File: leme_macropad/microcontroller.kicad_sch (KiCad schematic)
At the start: 23 parts, among them U3 W25Q128JVS, U4 RP2040, Y1 ABM8-272-T3

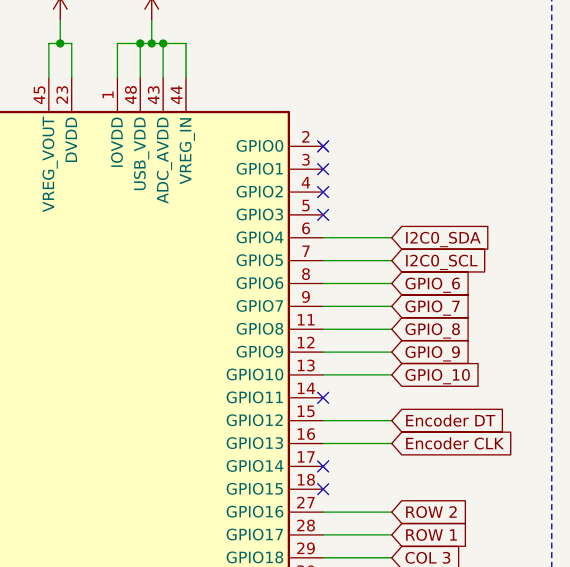
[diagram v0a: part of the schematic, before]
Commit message: Removes unused tespoints
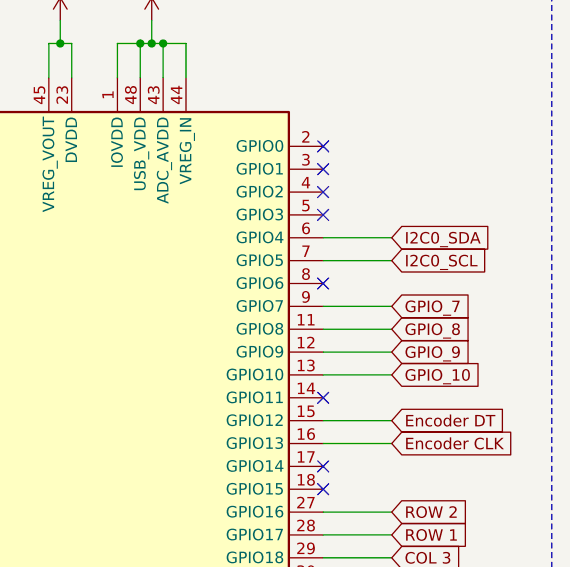
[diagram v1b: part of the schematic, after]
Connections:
- net GPIO_6: no longer names the net of U4.8 (GPIO6)
- no-connect marks 14 -> 15
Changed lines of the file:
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@@
+	)
+	(no_connect
+		(at 256.54 68.58)
 	)
 	(no_connect
@@
 	(wire
 		(pts
-			(xy 256.54 68.58) (xy 264.16 68.58)
-		)
-		(stroke
-			(width 0)
-			(type default)
-		)
-	)
-	(wire
-		(pts
 			(xy 199.39 109.22) (xy 205.74 109.22)
 		)
@@
 				(hide yes)
 			)
-		)
-	)
-	(global_label "GPIO_6"
-		(shape input)
-		(at 264.16 68.58 0)
-		(fields_autoplaced yes)
-		(effects
-			(font
-				(size 1.27 1.27)
-			)
-			(justify left)
-		)
-		(property "Intersheetrefs" "${INTERSHEET_REFS}"
-			(at 273.7976 68.58 0)
-			(effects
-				(font
-					(size 1.27 1.27)
-				)
-				(justify left)
-				(hide yes)
-			)

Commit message: Reassigns designators based on component location on the PCB
Kicad 6 has a tool for that: geographical reannotate.
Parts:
- renumbered C4 to C0, C12 to C1, C11 to C10, C10 to C11, C13 to C12, C15 to C13, C6 to C15, C7 to C16, C5 to C2, C16 to C3, C17 to C4, C3 to C5, C8 to C7, R5 to R0, R4 to R3, R6 to R5, R7 to R6, R3 to R7, U3 to U0, U4 to U3, Y1 to Y0
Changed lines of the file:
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@@
 		(on_board yes)
 		(dnp no)
-		(property "Reference" "C4"
+		(property "Reference" "C0"
 			(at 34.29 40.6462 0)
 			(effects
@@
 			(project "leme_macropad"
 				(path "/a37365a2-c635-4451-9354-78f9e753d687/97412fdd-d1b0-4c2a-b51e-7c921020fa0a"
-					(reference "C4")
+					(reference "C0")
 					(unit 1)
 				)
@@
 		(dnp no)
 		(fields_autoplaced yes)
-		(property "Reference" "R5"
+		(property "Reference" "R0"
 			(at 121.92 39.3699 0)
 			(effects
@@
 			(project "leme_macropad"
 				(path "/a37365a2-c635-4451-9354-78f9e753d687/97412fdd-d1b0-4c2a-b51e-7c921020fa0a"
-					(reference "R5")
+					(reference "R0")
 					(unit 1)
 				)
@@
 		(on_board yes)
 		(dnp no)
-		(property "Reference" "R6"
+		(property "Reference" "R5"
 			(at 192.024 58.928 90)
 			(effects
@@
 			(project "leme_macropad"
 				(path "/a37365a2-c635-4451-9354-78f9e753d687/97412fdd-d1b0-4c2a-b51e-7c921020fa0a"
-					(reference "R6")
+					(reference "R5")
 					(unit 1)
 				)
@@
 		(on_board yes)
 		(dnp no)
-		(property "Reference" "C6"
+		(property "Reference" "C15"
 			(at 41.9162 82.55 0)
 			(effects
@@
 			(project "leme_macropad"
 				(path "/a37365a2-c635-4451-9354-78f9e753d687/97412fdd-d1b0-4c2a-b51e-7c921020fa0a"
-					(reference "C6")
+					(reference "C15")
 					(unit 1)
 				)
@@
 		(on_board yes)
 		(dnp no)
-		(property "Reference" "C12"
+		(property "Reference" "C1"
 			(at 102.87 140.9762 0)
 			(effects
@@
 			(project "leme_macropad"
 				(path "/a37365a2-c635-4451-9354-78f9e753d687/97412fdd-d1b0-4c2a-b51e-7c921020fa0a"
-					(reference "C12")
+					(reference "C1")
 					(unit 1)
 				)
@@
 		(on_board yes)
 		(dnp no)
-		(property "Reference" "C8"
+		(property "Reference" "C7"
 			(at 52.07 167.6462 0)
 			(effects
@@
 			(project "leme_macropad"
 				(path "/a37365a2-c635-4451-9354-78f9e753d687/97412fdd-d1b0-4c2a-b51e-7c921020fa0a"
-					(reference "C8")
+					(reference "C7")
 					(unit 1)
 				)
@@
 		(dnp no)
 		(fields_autoplaced yes)
-		(property "Reference" "U3"
+		(property "Reference" "U0"
 			(at 58.42 40.6399 0)
 			(effects
@@
 			(project "leme_macropad"
 				(path "/a37365a2-c635-4451-9354-78f9e753d687/97412fdd-d1b0-4c2a-b51e-7c921020fa0a"
-					(reference "U3")
+					(reference "U0")
 					(unit 1)
 				)
@@
 		(on_board yes)
 		(dnp no)
-		(property "Reference" "R7"
+		(property "Reference" "R6"
 			(at 192.024 65.786 90)
 			(effects
@@
 			(project "leme_macropad"
 				(path "/a37365a2-c635-4451-9354-78f9e753d687/97412fdd-d1b0-4c2a-b51e-7c921020fa0a"
-					(reference "R7")
+					(reference "R6")
 					(unit 1)
 				)
@@
 		(on_board yes)
 		(dnp no)
-		(property "Reference" "C7"
+		(property "Reference" "C16"
 			(at 41.9162 105.41 0)
 			(effects
@@
 			(project "leme_macropad"
 				(path "/a37365a2-c635-4451-9354-78f9e753d687/97412fdd-d1b0-4c2a-b51e-7c921020fa0a"
-					(reference "C7")
+					(reference "C16")
 					(unit 1)
 				)
@@
 		(on_board yes)
 		(dnp no)
-		(property "Reference" "C16"
+		(property "Reference" "C3"
 			(at 128.27 140.9762 0)
 			(effects
@@
 			(project "leme_macropad"
 				(path "/a37365a2-c635-4451-9354-78f9e753d687/97412fdd-d1b0-4c2a-b51e-7c921020fa0a"
-					(reference "C16")
+					(reference "C3")
 					(unit 1)
 				)
@@
 		(on_board yes)
 		(dnp no)
-		(property "Reference" "C15"
+		(property "Reference" "C13"
 			(at 115.57 167.6462 0)
 			(effects
@@
 			(project "leme_macropad"
 				(path "/a37365a2-c635-4451-9354-78f9e753d687/97412fdd-d1b0-4c2a-b51e-7c921020fa0a"
-					(reference "C15")
+					(reference "C13")
 					(unit 1)
 				)
@@
 		(on_board yes)
 		(dnp no)
-		(property "Reference" "C3"
+		(property "Reference" "C5"
 			(at 26.67 167.6462 0)
 			(effects
@@
 			(project "leme_macropad"
 				(path "/a37365a2-c635-4451-9354-78f9e753d687/97412fdd-d1b0-4c2a-b51e-7c921020fa0a"
-					(reference "C3")
+					(reference "C5")
 					(unit 1)
 				)
@@
 		(on_board yes)
 		(dnp no)
-		(property "Reference" "C17"
+		(property "Reference" "C4"
 			(at 128.27 167.6462 0)
 			(effects
@@
 			(project "leme_macropad"
 				(path "/a37365a2-c635-4451-9354-78f9e753d687/97412fdd-d1b0-4c2a-b51e-7c921020fa0a"
-					(reference "C17")
+					(reference "C4")
 					(unit 1)
 				)
@@
 		(dnp no)
 		(fields_autoplaced yes)
-		(property "Reference" "R4"
+		(property "Reference" "R3"
 			(at 121.92 26.6699 0)
 			(effects
@@
 			(project "leme_macropad"
 				(path "/a37365a2-c635-4451-9354-78f9e753d687/97412fdd-d1b0-4c2a-b51e-7c921020fa0a"
-					(reference "R4")
+					(reference "R3")
 					(unit 1)
 				)
@@
 		(dnp no)
 		(fields_autoplaced yes)
-		(property "Reference" "U4"
+		(property "Reference" "U3"
 			(at 233.2833 135.89 0)
 			(effects
@@
 			(project "leme_macropad"
 				(path "/a37365a2-c635-4451-9354-78f9e753d687/97412fdd-d1b0-4c2a-b51e-7c921020fa0a"
-					(reference "U4")
+					(reference "U3")
 					(unit 1)
 				)
@@
 		(on_board yes)
 		(dnp no)
-		(property "Reference" "R3"
+		(property "Reference" "R7"
 			(at 75.184 105.156 90)
 			(effects
@@
 			(project "leme_macropad"
 				(path "/a37365a2-c635-4451-9354-78f9e753d687/97412fdd-d1b0-4c2a-b51e-7c921020fa0a"
-					(reference "R3")
+					(reference "R7")
 					(unit 1)
 				)
@@
 		(on_board yes)
 		(dnp no)
-		(property "Reference" "C11"
+		(property "Reference" "C10"
 			(at 90.17 167.6462 0)
 			(effects
@@
 			(project "leme_macropad"
 				(path "/a37365a2-c635-4451-9354-78f9e753d687/97412fdd-d1b0-4c2a-b51e-7c921020fa0a"
-					(reference "C11")
+					(reference "C10")
 					(unit 1)
 				)
@@
 		(on_board yes)
 		(dnp no)
-		(property "Reference" "Y1"
+		(property "Reference" "Y0"
 			(at 64.77 96.012 90)
 			(effects
@@
 			(project "leme_macropad"
 				(path "/a37365a2-c635-4451-9354-78f9e753d687/97412fdd-d1b0-4c2a-b51e-7c921020fa0a"
-					(reference "Y1")
+					(reference "Y0")
 					(unit 1)
 				)
@@
 		(on_board yes)
 		(dnp no)
-		(property "Reference" "C10"
+		(property "Reference" "C11"
 			(at 77.47 167.6462 0)
 			(effects
@@
 			(project "leme_macropad"
 				(path "/a37365a2-c635-4451-9354-78f9e753d687/97412fdd-d1b0-4c2a-b51e-7c921020fa0a"
-					(reference "C10")
+					(reference "C11")
 					(unit 1)
 				)
@@
 		(on_board yes)
 		(dnp no)
-		(property "Reference" "C13"
+		(property "Reference" "C12"
 			(at 102.87 167.6462 0)
 			(effects
@@
 			(project "leme_macropad"
 				(path "/a37365a2-c635-4451-9354-78f9e753d687/97412fdd-d1b0-4c2a-b51e-7c921020fa0a"
-					(reference "C13")
+					(reference "C12")
 					(unit 1)
 				)
@@
 		(on_board yes)
 		(dnp no)
-		(property "Reference" "C5"
+		(property "Reference" "C2"
 			(at 39.37 167.6462 0)
 			(effects
@@
 			(project "leme_macropad"
 				(path "/a37365a2-c635-4451-9354-78f9e753d687/97412fdd-d1b0-4c2a-b51e-7c921020fa0a"
-					(reference "C5")
-					(unit 1)
-				)
+					(reference "C2")
+					(unit 1)
+				)

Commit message: Adds i2c pull-up resistors that were missing (!)
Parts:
- added R11, R12: 10kΩ, Resistor_SMD:R_0402_1005Metric_Pad0.72x0.64mm_HandSolder, symbol Device:R_Small_US
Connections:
- net +3.3V: now also R11.2, R12.2
- net I2C0_SCL: now also R11.1
- net I2C0_SDA: now also R12.1

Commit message: Moves SDA/SCL i2c pins to make it easier to route
This also required moving the encoder pins, which will also make them
easier to route with this placement of the RP2040.

This commit also changes the configuration for QMK to use the new pins.
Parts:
- removed R11, R12: 10kΩ, Resistor_SMD:R_0402_1005Metric_Pad0.72x0.64mm_HandSolder, symbol Device:R_Small_US
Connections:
- net Encoder CLK: now also U3.4 (GPIO2); no longer U3.16 (GPIO13)
- net Encoder DT: now also U3.5 (GPIO3); no longer U3.15 (GPIO12)
- net I2C0_SCL: now also U3.16 (GPIO13); no longer U3.7 (GPIO5)
- net I2C0_SDA: now also U3.15 (GPIO12); no longer U3.6 (GPIO4)

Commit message: Changes the matrix pins hoping it will make them easier to route
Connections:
- net COL 1: now also U3.8 (GPIO6); no longer U3.31 (GPIO20)
- net COL 2: now also U3.7 (GPIO5); no longer U3.30 (GPIO19)
- net COL 3: now also U3.6 (GPIO4); no longer U3.29 (GPIO18)
- net COL 4: now also U3.3 (GPIO1); no longer U3.32 (GPIO21)
- net Encoder CLK: now also U3.5 (GPIO3); no longer U3.4 (GPIO2)
- net Encoder DT: now also U3.4 (GPIO2); no longer U3.5 (GPIO3)
- net GPIO_10: now also U3.32 (GPIO21); no longer U3.13 (GPIO10)
- net GPIO_7: now also U3.29 (GPIO18); no longer U3.9 (GPIO7)
- net GPIO_8: now also U3.30 (GPIO19); no longer U3.11 (GPIO8)
- net GPIO_9: now also U3.31 (GPIO20); no longer U3.12 (GPIO9)
- net ROW 1: now also U3.13 (GPIO10); no longer U3.28 (GPIO17)
- net ROW 2: now also U3.14 (GPIO11); no longer U3.27 (GPIO16)

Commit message: Changes ws2812 data pin
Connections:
- net LED_DATA_IN: now also U3.12 (GPIO9); no longer U3.34 (GPIO22)
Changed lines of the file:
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@@
 	)
 	(no_connect
-		(at 256.54 76.2)
+		(at 256.54 109.22)
 	)
 	(no_connect
@@
 	(wire
 		(pts
-			(xy 256.54 109.22) (xy 264.16 109.22)
+			(xy 256.54 76.2) (xy 264.16 76.2)
 		)
 		(stroke
@@
 	(global_label "LED_DATA_IN"
 		(shape input)
-		(at 264.16 109.22 0)
-		(fields_autoplaced yes)
-		(effects
-			(font
-				(size 1.27 1.27)
-			)
-			(justify left)
-		)
-		(property "Intersheetrefs" "${INTERSHEET_REFS}"
-			(at 278.8776 109.22 0)
-			(effects
-				(font
+		(at 264.16 76.2 0)
+		(fields_autoplaced yes)
+		(effects
+			(font
+				(size 1.27 1.27)
+			)
+			(justify left)
+		)
+		(property "Intersheetrefs" "${INTERSHEET_REFS}"
+			(at 278.8776 76.2 0)
+			(effects
+				(font

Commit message: Geographically reanotates component designators
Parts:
- renumbered C5 to C0, C7 to C1, C2 to C10, C16 to C11, C1 to C12, C15 to C13, C9 to C14, C11 to C15, C0 to C16, C10 to C2, C12 to C3, C4 to C5, C3 to C7, C14 to C8, C13 to C9, R6 to R3, R5 to R4, R7 to R5, R3 to R6, R0 to R7, U3 to U1, U0 to U3
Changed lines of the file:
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@@
 		(on_board yes)
 		(dnp no)
-		(property "Reference" "C0"
+		(property "Reference" "C16"
 			(at 34.29 40.6462 0)
 			(effects
@@
 			(project "leme_macropad"
 				(path "/a37365a2-c635-4451-9354-78f9e753d687/97412fdd-d1b0-4c2a-b51e-7c921020fa0a"
-					(reference "C0")
+					(reference "C16")
 					(unit 1)
 				)
@@
 		(dnp no)
 		(fields_autoplaced yes)
-		(property "Reference" "R0"
+		(property "Reference" "R7"
 			(at 121.92 39.3699 0)
 			(effects
@@
 			(project "leme_macropad"
 				(path "/a37365a2-c635-4451-9354-78f9e753d687/97412fdd-d1b0-4c2a-b51e-7c921020fa0a"
-					(reference "R0")
+					(reference "R7")
 					(unit 1)
 				)
@@
 		(on_board yes)
 		(dnp no)
-		(property "Reference" "R5"
+		(property "Reference" "R4"
 			(at 192.024 58.928 90)
 			(effects
@@
 			(project "leme_macropad"
 				(path "/a37365a2-c635-4451-9354-78f9e753d687/97412fdd-d1b0-4c2a-b51e-7c921020fa0a"
-					(reference "R5")
+					(reference "R4")
 					(unit 1)
 				)
@@
 		(on_board yes)
 		(dnp no)
-		(property "Reference" "C15"
+		(property "Reference" "C13"
 			(at 41.9162 82.55 0)
 			(effects
@@
 			(project "leme_macropad"
 				(path "/a37365a2-c635-4451-9354-78f9e753d687/97412fdd-d1b0-4c2a-b51e-7c921020fa0a"
-					(reference "C15")
+					(reference "C13")
 					(unit 1)
 				)
@@
 		(on_board yes)
 		(dnp no)
-		(property "Reference" "C1"
+		(property "Reference" "C12"
 			(at 102.87 140.9762 0)
 			(effects
@@
 			(project "leme_macropad"
 				(path "/a37365a2-c635-4451-9354-78f9e753d687/97412fdd-d1b0-4c2a-b51e-7c921020fa0a"
-					(reference "C1")
+					(reference "C12")
 					(unit 1)
 				)
@@
 		(on_board yes)
 		(dnp no)
-		(property "Reference" "C7"
+		(property "Reference" "C1"
 			(at 52.07 167.6462 0)
 			(effects
@@
 			(project "leme_macropad"
 				(path "/a37365a2-c635-4451-9354-78f9e753d687/97412fdd-d1b0-4c2a-b51e-7c921020fa0a"
-					(reference "C7")
+					(reference "C1")
 					(unit 1)
 				)
@@
 		(dnp no)
 		(fields_autoplaced yes)
-		(property "Reference" "U0"
+		(property "Reference" "U3"
 			(at 58.42 40.6399 0)
 			(effects
@@
 			(project "leme_macropad"
 				(path "/a37365a2-c635-4451-9354-78f9e753d687/97412fdd-d1b0-4c2a-b51e-7c921020fa0a"
-					(reference "U0")
+					(reference "U3")
 					(unit 1)
 				)
@@
 		(on_board yes)
 		(dnp no)
-		(property "Reference" "R6"
+		(property "Reference" "R3"
 			(at 192.024 65.786 90)
 			(effects
@@
 			(project "leme_macropad"
 				(path "/a37365a2-c635-4451-9354-78f9e753d687/97412fdd-d1b0-4c2a-b51e-7c921020fa0a"
-					(reference "R6")
+					(reference "R3")
 					(unit 1)
 				)
@@
 		(on_board yes)
 		(dnp no)
-		(property "Reference" "C9"
+		(property "Reference" "C14"
 			(at 64.77 167.6462 0)
 			(effects
@@
 			(project "leme_macropad"
 				(path "/a37365a2-c635-4451-9354-78f9e753d687/97412fdd-d1b0-4c2a-b51e-7c921020fa0a"
-					(reference "C9")
+					(reference "C14")
 					(unit 1)
 				)
@@
 		(on_board yes)
 		(dnp no)
-		(property "Reference" "C16"
+		(property "Reference" "C11"
 			(at 41.9162 105.41 0)
 			(effects
@@
 			(project "leme_macropad"
 				(path "/a37365a2-c635-4451-9354-78f9e753d687/97412fdd-d1b0-4c2a-b51e-7c921020fa0a"
-					(reference "C16")
+					(reference "C11")
 					(unit 1)
 				)
@@
 		(on_board yes)
 		(dnp no)
-		(property "Reference" "C3"
+		(property "Reference" "C7"
 			(at 128.27 140.9762 0)
 			(effects
@@
 			(project "leme_macropad"
 				(path "/a37365a2-c635-4451-9354-78f9e753d687/97412fdd-d1b0-4c2a-b51e-7c921020fa0a"
-					(reference "C3")
+					(reference "C7")
 					(unit 1)
 				)
@@
 		(on_board yes)
 		(dnp no)
-		(property "Reference" "C13"
+		(property "Reference" "C9"
 			(at 115.57 167.6462 0)
 			(effects
@@
 			(project "leme_macropad"
 				(path "/a37365a2-c635-4451-9354-78f9e753d687/97412fdd-d1b0-4c2a-b51e-7c921020fa0a"
-					(reference "C13")
+					(reference "C9")
 					(unit 1)
 				)
@@
 		(on_board yes)
 		(dnp no)
-		(property "Reference" "C5"
+		(property "Reference" "C0"
 			(at 26.67 167.6462 0)
 			(effects
@@
 			(project "leme_macropad"
 				(path "/a37365a2-c635-4451-9354-78f9e753d687/97412fdd-d1b0-4c2a-b51e-7c921020fa0a"
-					(reference "C5")
+					(reference "C0")
 					(unit 1)
 				)
@@
 		(on_board yes)
 		(dnp no)
-		(property "Reference" "C4"
+		(property "Reference" "C5"
 			(at 128.27 167.6462 0)
 			(effects
@@
 			(project "leme_macropad"
 				(path "/a37365a2-c635-4451-9354-78f9e753d687/97412fdd-d1b0-4c2a-b51e-7c921020fa0a"
-					(reference "C4")
+					(reference "C5")
 					(unit 1)
 				)
@@
 		(dnp no)
 		(fields_autoplaced yes)
-		(property "Reference" "R3"
+		(property "Reference" "R6"
 			(at 121.92 26.6699 0)
 			(effects
@@
 			(project "leme_macropad"
 				(path "/a37365a2-c635-4451-9354-78f9e753d687/97412fdd-d1b0-4c2a-b51e-7c921020fa0a"
-					(reference "R3")
+					(reference "R6")
 					(unit 1)
 				)
@@
 		(dnp no)
 		(fields_autoplaced yes)
-		(property "Reference" "U3"
+		(property "Reference" "U1"
 			(at 233.2833 135.89 0)
 			(effects
@@
 			(project "leme_macropad"
 				(path "/a37365a2-c635-4451-9354-78f9e753d687/97412fdd-d1b0-4c2a-b51e-7c921020fa0a"
-					(reference "U3")
+					(reference "U1")
 					(unit 1)
 				)
@@
 		(on_board yes)
 		(dnp no)
-		(property "Reference" "R7"
+		(property "Reference" "R5"
 			(at 75.184 105.156 90)
 			(effects
@@
 			(project "leme_macropad"
 				(path "/a37365a2-c635-4451-9354-78f9e753d687/97412fdd-d1b0-4c2a-b51e-7c921020fa0a"
-					(reference "R7")
+					(reference "R5")
 					(unit 1)
 				)
@@
 		(on_board yes)
 		(dnp no)
-		(property "Reference" "C10"
+		(property "Reference" "C2"
 			(at 90.17 167.6462 0)
 			(effects
@@
 			(project "leme_macropad"
 				(path "/a37365a2-c635-4451-9354-78f9e753d687/97412fdd-d1b0-4c2a-b51e-7c921020fa0a"
-					(reference "C10")
+					(reference "C2")
 					(unit 1)
 				)
@@
 		(on_board yes)
 		(dnp no)
-		(property "Reference" "C11"
+		(property "Reference" "C15"
 			(at 77.47 167.6462 0)
 			(effects
@@
 			(project "leme_macropad"
 				(path "/a37365a2-c635-4451-9354-78f9e753d687/97412fdd-d1b0-4c2a-b51e-7c921020fa0a"
-					(reference "C11")
+					(reference "C15")
 					(unit 1)
 				)
@@
 		(on_board yes)
 		(dnp no)
-		(property "Reference" "C14"
+		(property "Reference" "C8"
 			(at 115.57 140.9762 0)
 			(effects
@@
 			(project "leme_macropad"
 				(path "/a37365a2-c635-4451-9354-78f9e753d687/97412fdd-d1b0-4c2a-b51e-7c921020fa0a"
-					(reference "C14")
+					(reference "C8")
 					(unit 1)
 				)
@@
 		(on_board yes)
 		(dnp no)
-		(property "Reference" "C12"
+		(property "Reference" "C3"
 			(at 102.87 167.6462 0)
 			(effects
@@
 			(project "leme_macropad"
 				(path "/a37365a2-c635-4451-9354-78f9e753d687/97412fdd-d1b0-4c2a-b51e-7c921020fa0a"
-					(reference "C12")
+					(reference "C3")
 					(unit 1)
 				)
@@
 		(on_board yes)
 		(dnp no)
-		(property "Reference" "C2"
+		(property "Reference" "C10"
 			(at 39.37 167.6462 0)
 			(effects
@@
 			(project "leme_macropad"
 				(path "/a37365a2-c635-4451-9354-78f9e753d687/97412fdd-d1b0-4c2a-b51e-7c921020fa0a"
-					(reference "C2")
-					(unit 1)
-				)
+					(reference "C10")
+					(unit 1)
+				)
